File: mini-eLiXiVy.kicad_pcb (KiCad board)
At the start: 2 copper layers, 302.2 x 93.5 mm, 175 parts, among them J1 TYPE-C-31-M12_13_EDITED, J2 AVR-ISP-6, SW1 SW_Push, U1 ATmega32U4-AU, U2 WE-TVS-82400102, Y1 Crystal_GND24_Small

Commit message: modified repo text and branding etc
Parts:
- removed LO1: mini-eLiXiVy-Mask, mini-Logos:eLiXiVy-rev1.1-Mask
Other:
- net class Default removed
- net class Power removed

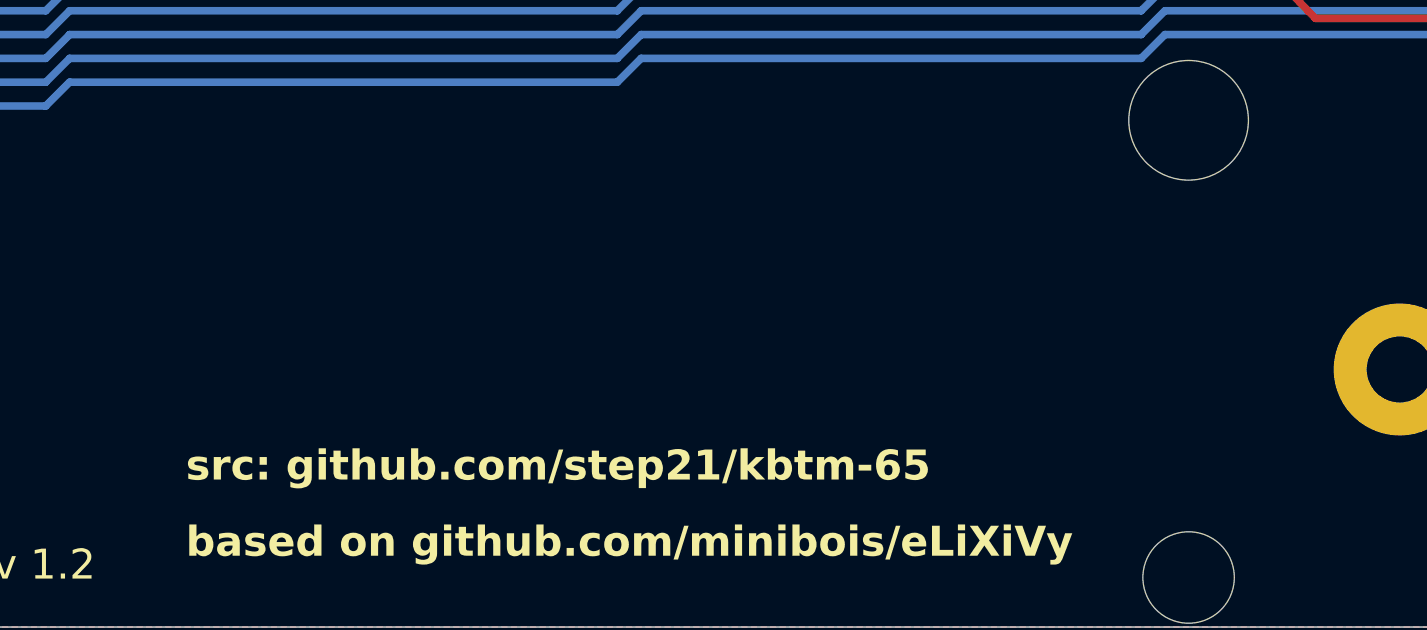
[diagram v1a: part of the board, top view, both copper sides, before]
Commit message: placed bmc labs logo
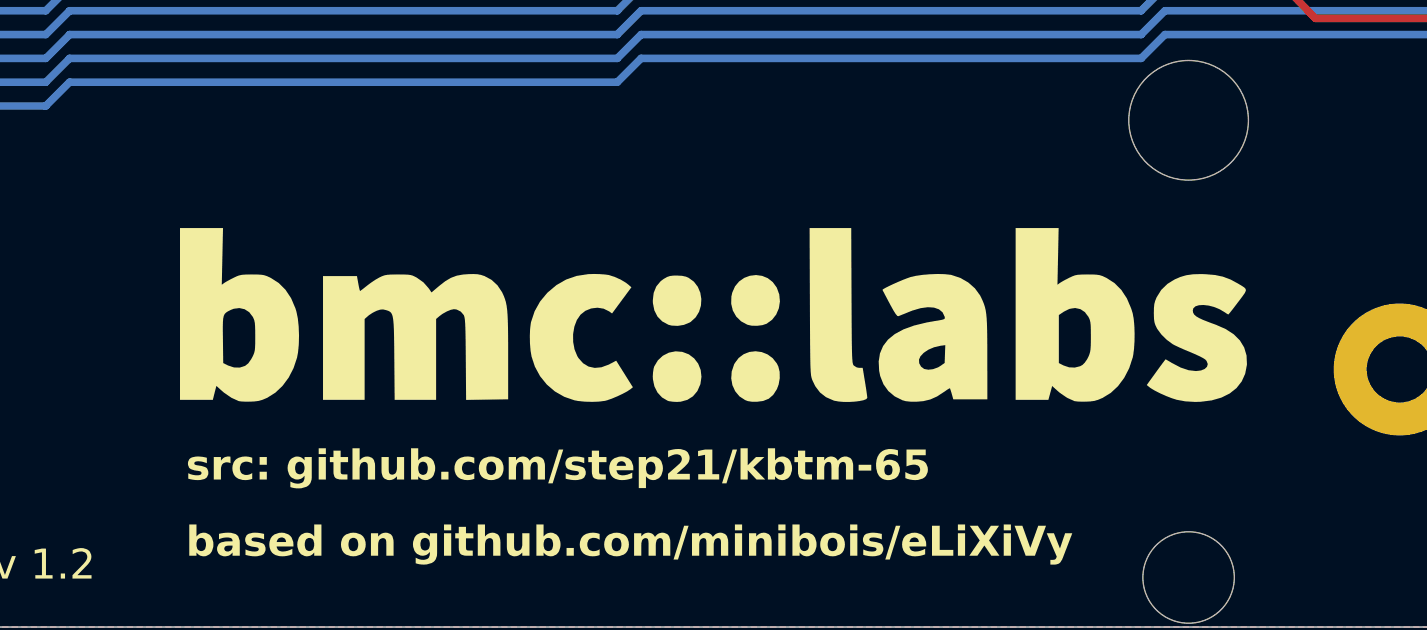
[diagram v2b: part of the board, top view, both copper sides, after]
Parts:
- added G***: LOGO, bmc_labs:bmclabs_footprint, F.Cu at (177.8, 99.1)
